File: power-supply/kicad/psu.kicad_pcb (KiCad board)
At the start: 2 copper layers, 22 x 21.6 mm, 13 parts, among them J3 SSQ-103-03-G-D, U1 LM2776, U3 TPS72301DBVR, U5 TPS79333DBVR

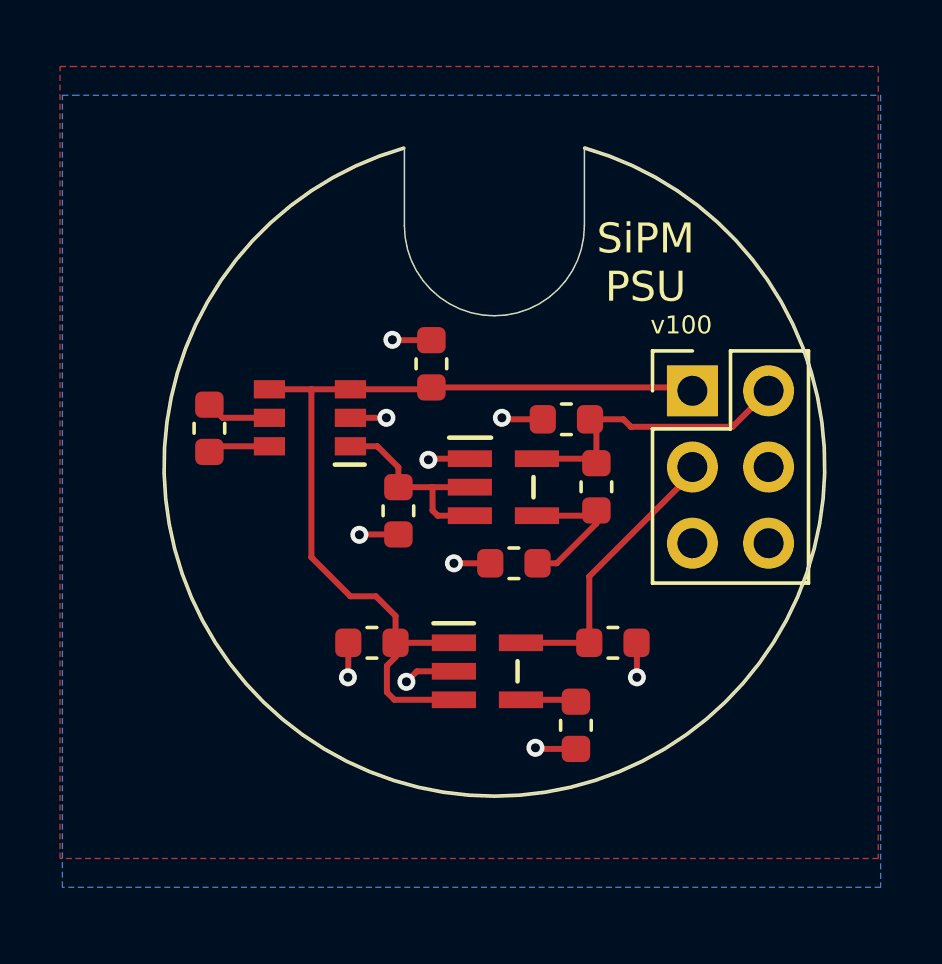
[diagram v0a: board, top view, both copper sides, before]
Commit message: Minor changes to power supply
Changes:

Add LC filter on output of the negative regulator. This is almost certainly not needed, but it further rejects the 2MHz inverting regulator switch frequency.  Replace inductor with a jumper if you don't want to use it.

Clean up traces and layout of existing components.

Widen notch so that SMB cables can fit through more easily.

Adjust negative rail voltage to be -4.5v instead of -3.3v to increase dynamic range.

Move connector so there is a bit more room to fit in lens tube.
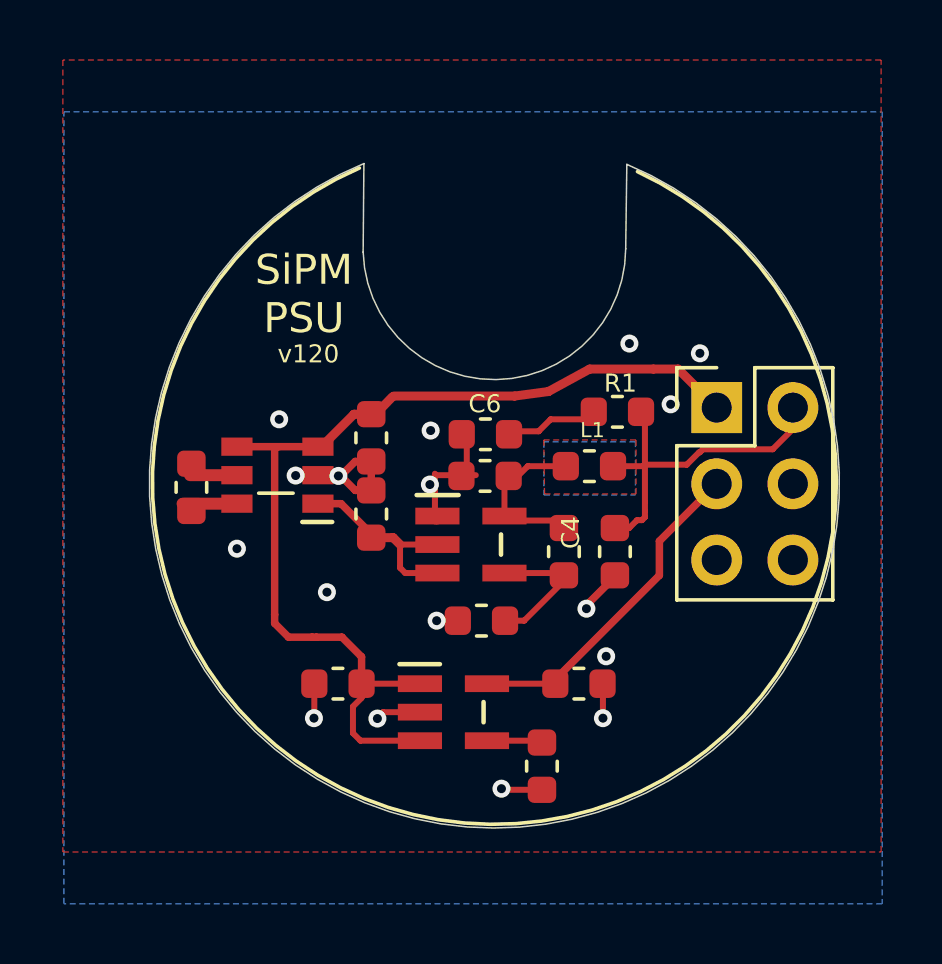
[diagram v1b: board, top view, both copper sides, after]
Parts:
- added C4: 22u, footprints:C_0603_1608Metric, F.Cu at (204.0, 102.9)
- added C6: 22u, footprints:C_0603_1608Metric, F.Cu at (199.7, 99.0)
- added L1: 1uH, footprints:L_0603_1608Metric, F.Cu at (203.2, 100.0)
- added R1: .5, footprints:R_0603_1608Metric, F.Cu at (204.1, 98.2)
- C2: value 10u -> 1u
- C3, C5: value 10u -> 22u
- U3: value TPS72301DBVR -> DBV5
- U5: value TPS79333DBVR -> DBV5
- moved C5 3.30 mm to (199.7, 100.3)
- moved C1 3.18 mm to (195.9, 99.1), turned to 90 degrees
- moved R8 2.42 mm to (202.3, 102.9)
- moved R9 2.20 mm to (199.6, 105.2)
- moved U1 2.20 mm to (192.8, 100.3)
- moved U3 2.20 mm to (199.2, 102.6)
- moved C8 2.06 mm to (189.9, 100.7)
- moved C17 1.77 mm to (201.6, 110.0)
- moved C2 1.77 mm to (194.8, 107.3)
- moved C3 1.77 mm to (202.8, 107.3)
- moved U5 1.77 mm to (198.6, 108.2)
- moved J3 0.98 mm to (207.4, 98.1)
- moved C15 0.91 mm to (195.9, 101.6), turned to -90 degrees
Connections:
- C5 pad 2: VSSA -> Net-(C5-Pad2)
- J3 pad 4: (no net) -> Net-(J3-Pad4)
- J3 pad 5: (no net) -> /BIAS
- R8 pad 2: VSSA -> Net-(C5-Pad2)
- U3 pad 5: VSSA -> Net-(C5-Pad2)
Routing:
- net Net-(C5-Pad2): track 0.00 -> 5.48 mm
- net GND: track 13.3 -> 16.7 mm, vias 10 -> 17
- net Net-(C6-Pad1): track 0.00 -> 3.32 mm
- net +5V: track 30.7 -> 33.6 mm
- net VSSA: track 9.85 -> 12.0 mm
- net VDDA: track 10.7 -> 12.0 mm
- net Net-(C8-Pad2): track 2.38 -> 1.56 mm
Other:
- board size 22 x 21.6 mm -> 23 x 22.1 mm
- net class Default removed
- board text added: "+3.3V"
- board text added: "-4.5V"
- board text added: "Bias"
- board text added: "GND"
- board text added: "USB5V"
- board text added: "v120"
- board text removed: "v100"

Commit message: Lower negative voltage rail slightly
Depending on the USB +5 load, the length of the cable, etc the voltage could dip enough that the regulator would drop out under very heavy load.  Decreasing to 4.3v prevents this but still enables >1.3v output.
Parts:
- C4: value 22u -> 4.7u
- R9: value 36.5k -> 24.9k
- U3: value DBV5 -> TPS72301DBVR
- U5: value DBV5 -> TPS79333DBVR
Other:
- board text added: "-4.3V"
- board text removed: "-4.5V"
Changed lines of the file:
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@@
     (fp_circle (center -0.5461 -0.95) (end -0.4699 -0.95) (layer "F.Fab") (width 0.1524))
     (pad "1" smd rect (at -1.35 -0.950001 180) (size 1.0414 0.6096) (layers "F.Cu" "F.Paste" "F.Mask")
-      (net 4 "-5V"))
+      (net 4 "-5V") (pinfunction "Vout"))
     (pad "2" smd rect (at -1.35 0 180) (size 1.0414 0.6096) (layers "F.Cu" "F.Paste" "F.Mask")
-      (net 1 "GND"))
+      (net 1 "GND") (pinfunction "GND"))
     (pad "3" smd rect (at -1.35 0.950001 180) (size 1.0414 0.6096) (layers "F.Cu" "F.Paste" "F.Mask")
-      (net 2 "+5V"))
+      (net 2 "+5V") (pinfunction "Vin"))
     (pad "4" smd rect (at 1.35 0.950001 180) (size 1.0414 0.6096) (layers "F.Cu" "F.Paste" "F.Mask")
-      (net 2 "+5V"))
+      (net 2 "+5V") (pinfunction "EN"))
     (pad "5" smd rect (at 1.35 0 180) (size 1.0414 0.6096) (layers "F.Cu" "F.Paste" "F.Mask")
-      (net 6 "Net-(C8-Pad2)"))
+      (net 6 "Net-(C8-Pad2)") (pinfunction "C1+"))
     (pad "6" smd rect (at 1.35 -0.950001 180) (size 1.0414 0.6096) (layers "F.Cu" "F.Paste" "F.Mask")
-      (net 7 "Net-(C8-Pad1)"))
+      (net 7 "Net-(C8-Pad1)") (pinfunction "C1-"))
     (model "${KIPRJMOD}/step/DBV6.step"
       (at (xyz 0 0 0))
@@
     (tags "inductor")
     (attr smd)
-    (fp_text reference "L1" (at -0.1 1.2) (layer "F.SilkS")
+    (fp_text reference "L1" (at 0.0176 -0.937499) (layer "F.SilkS")
       (effects (font (size 0.5 0.5) (thickness 0.1)))
     )
@@
     (tags "capacitor")
     (attr smd)
-    (fp_text reference "C4" (at -0.6375 1.475 -90) (layer "F.SilkS")
-      (effects (font (size 0.6 0.6) (thickness 0.1)))
-    )
-    (fp_text value "22u" (at 0 1.43 90) (layer "F.Fab")
+    (fp_text reference "C4" (at 1.962499 0.0426) (layer "F.SilkS")
+      (effects (font (size 0.6 0.6) (thickness 0.1)))
+    )
+    (fp_text value "4.7u" (at 0 1.43 90) (layer "F.Fab")
       (effects (font (size 0.6 0.6) (thickness 0.1)))
     )
@@
       (effects (font (size 1 1) (thickness 0.15)))
     )
-    (fp_text value "DBV5" (at 0 0) (layer "F.SilkS") hide
+    (fp_text value "TPS79333DBVR" (at 0 0) (layer "F.SilkS") hide
       (effects (font (size 1 1) (thickness 0.15)))
     )
@@
     )
     (pad "1" smd rect (at -1.1176 -0.950001) (size 1.4732 0.5588) (layers "F.Cu" "F.Paste" "F.Mask")
-      (net 2 "+5V"))
+      (net 2 "+5V") (pinfunction "IN"))
     (pad "2" smd rect (at -1.1176 0) (size 1.4732 0.5588) (layers "F.Cu" "F.Paste" "F.Mask")
-      (net 1 "GND"))
+      (net 1 "GND") (pinfunction "GND"))
     (pad "3" smd rect (at -1.1176 0.950001) (size 1.4732 0.5588) (layers "F.Cu" "F.Paste" "F.Mask")
-      (net 2 "+5V"))
+      (net 2 "+5V") (pinfunction "EN"))
     (pad "4" smd rect (at 1.1176 0.950001) (size 1.4732 0.5588) (layers "F.Cu" "F.Paste" "F.Mask")
-      (net 8 "Net-(C17-Pad2)"))
+      (net 8 "Net-(C17-Pad2)") (pinfunction "NR"))
     (pad "5" smd rect (at 1.1176 -0.950001) (size 1.4732 0.5588) (layers "F.Cu" "F.Paste" "F.Mask")
-      (net 3 "VDDA"))
+      (net 3 "VDDA") (pinfunction "OUT"))
     (model "${KIPRJMOD}/step/DBV5.step"
       (at (xyz 0 0 0))
@@
       (effects (font (size 1 1) (thickness 0.15)))
     )
-    (fp_text value "DBV5" (at 0 0) (layer "F.SilkS") hide
+    (fp_text value "TPS72301DBVR" (at 0 0) (layer "F.SilkS") hide
       (effects (font (size 1 1) (thickness 0.15)))
     )
@@
     )
     (pad "5" smd rect (at 1.1176 -0.950001) (size 1.4732 0.5588) (layers "F.Cu" "F.Paste" "F.Mask")
-      (net 10 "Net-(C5-Pad2)"))
+      (net 10 "Net-(C5-Pad2)") (pinfunction "OUT"))
     (pad "4" smd rect (at 1.1176 0.950001) (size 1.4732 0.5588) (layers "F.Cu" "F.Paste" "F.Mask")
-      (net 9 "Net-(R8-Pad1)"))
+      (net 9 "Net-(R8-Pad1)") (pinfunction "FB"))
     (pad "3" smd rect (at -1.1176 0.950001) (size 1.4732 0.5588) (layers "F.Cu" "F.Paste" "F.Mask")
-      (net 4 "-5V"))
+      (net 4 "-5V") (pinfunction "EN"))
     (pad "2" smd rect (at -1.1176 0) (size 1.4732 0.5588) (layers "F.Cu" "F.Paste" "F.Mask")
-      (net 4 "-5V"))
+      (net 4 "-5V") (pinfunction "IN"))
     (pad "1" smd rect (at -1.1176 -0.950001) (size 1.4732 0.5588) (layers "F.Cu" "F.Paste" "F.Mask")
-      (net 1 "GND"))
+      (net 1 "GND") (pinfunction "GND"))
     (model "${KIPRJMOD}/step/DBV5.step"
       (at (xyz 0 0 0))
@@
       (effects (font (size 0.6 0.6) (thickness 0.1)))
     )
-    (fp_text value "36.5k" (at 0 1.43) (layer "F.Fab") hide
+    (fp_text value "24.9k" (at 0 1.43) (layer "F.Fab") hide
       (effects (font (size 1 1) (thickness 0.15)))
     )
@@
     (tags "capacitor")
     (attr smd)
-    (fp_text reference "C3" (at -0.6375 1.475 180) (layer "F.SilkS") hide
+    (fp_text reference "C3" (at -0.0074 1.1375 180) (layer "F.SilkS") hide
       (effects (font (size 0.6 0.6) (thickness 0.1)))
     )
@@
     (fp_line (start 0 -1.27) (end 3.81 -1.27) (layer "F.Fab") (width 0.1))
     (pad "6" thru_hole oval (at 2.54 5.08) (size 1.7 1.7) (drill 1) (layers *.Cu *.Mask)
-      (net 1 "GND"))
+      (net 1 "GND") (pinfunction "Pin_6"))
     (pad "5" thru_hole oval (at 0 5.08) (size 1.7 1.7) (drill 1) (layers *.Cu *.Mask)
-      (net 11 "/BIAS"))
+      (net 11 "/BIAS") (pinfunction "Pin_5"))
     (pad "4" thru_hole oval (at 2.54 2.54) (size 1.7 1.7) (drill 1) (layers *.Cu *.Mask)
-      (net 12 "Net-(J3-Pad4)"))
+      (net 12 "Net-(J3-Pad4)") (pinfunction "Pin_4"))
     (pad "3" thru_hole oval (at 0 2.54) (size 1.7 1.7) (drill 1) (layers *.Cu *.Mask)
-      (net 3 "VDDA"))
+      (net 3 "VDDA") (pinfunction "Pin_3"))
     (pad "2" thru_hole oval (at 2.54 0) (size 1.7 1.7) (drill 1) (layers *.Cu *.Mask)
-      (net 5 "VSSA"))
+      (net 5 "VSSA") (pinfunction "Pin_2"))
     (pad "1" thru_hole rect (at 0 0) (size 1.7 1.7) (drill 1) (layers *.Cu *.Mask)
-      (net 2 "+5V"))
+      (net 2 "+5V") (pinfunction "Pin_1"))
     (model "${KIPRJMOD}/step/SSQ-103-03-G-D.step"
       (offset (xyz 1.25 -2.5 0))
@@
     (effects (font (size 1 1) (thickness 0.15)) (justify mirror))
   )
-  (gr_text "-4.5V" (at 209.3 96.1) (layer "B.SilkS")
+  (gr_text "-4.3V" (at 209.3 96.1) (layer "B.SilkS")
     (effects (font (size 0.6 0.6) (thickness 0.15)) (justify mirror))
   )

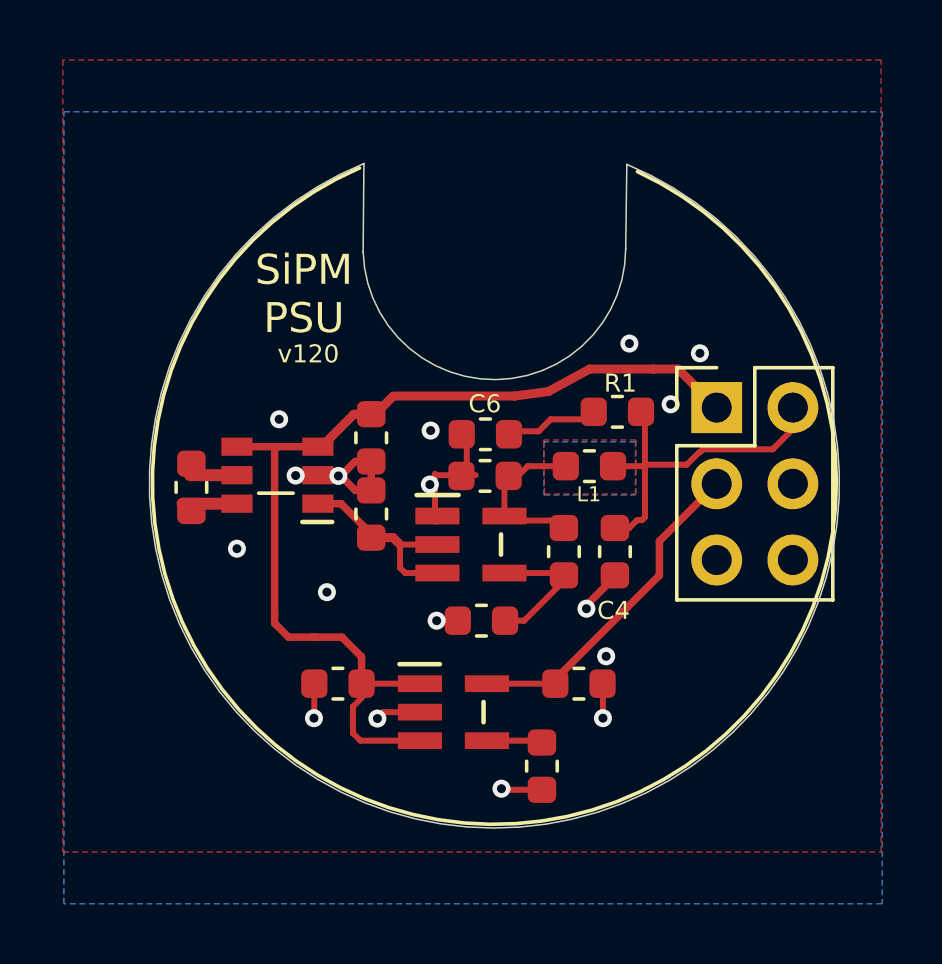
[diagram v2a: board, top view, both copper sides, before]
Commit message: Slightly improve routing around the nedative power supply
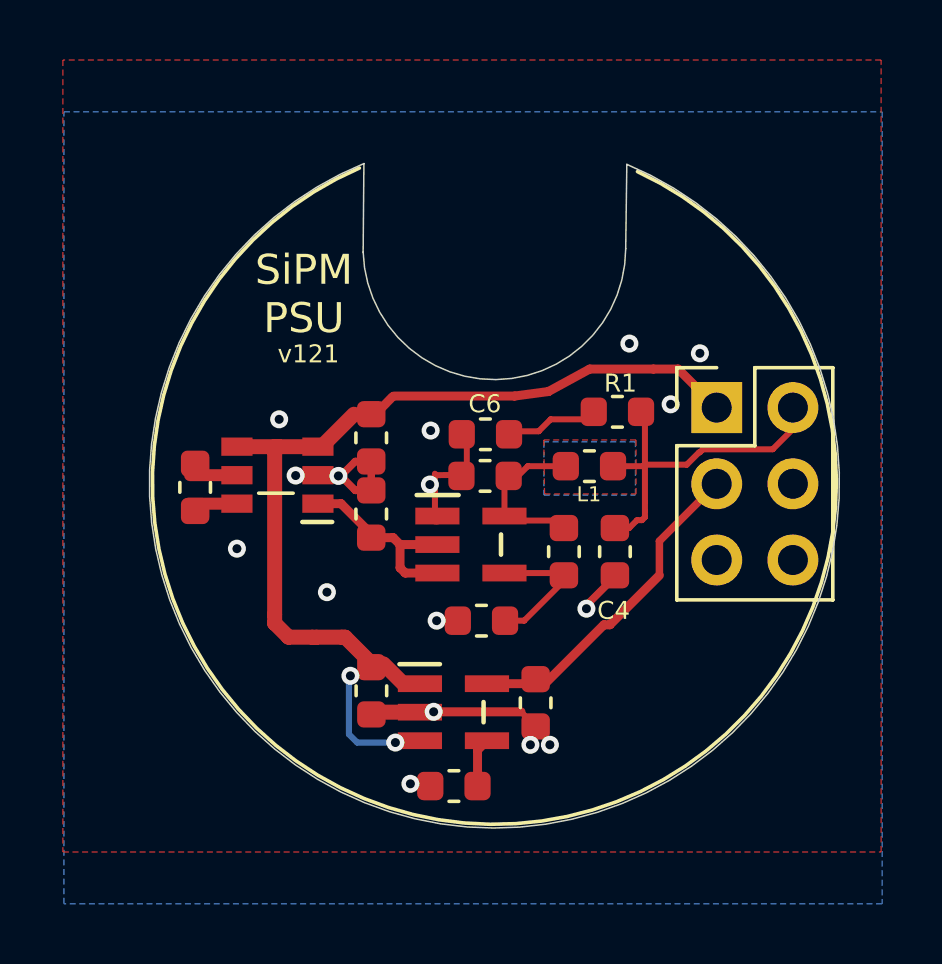
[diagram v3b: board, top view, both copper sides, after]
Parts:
- moved C17 3.01 mm to (198.7, 110.7), turned to 0 degrees
- moved C3 1.58 mm to (201.4, 107.9), turned to 90 degrees
- moved C2 1.14 mm to (195.9, 107.5), turned to 90 degrees
- moved C8 0.12 mm to (190.0, 100.7)
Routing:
- net GND: track 16.7 -> 15.8 mm, vias 17 -> 16
- net +5V: track 33.6 -> 32.9 mm, vias 0 -> 2
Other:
- board text added: "v121"
- board text removed: "v120"

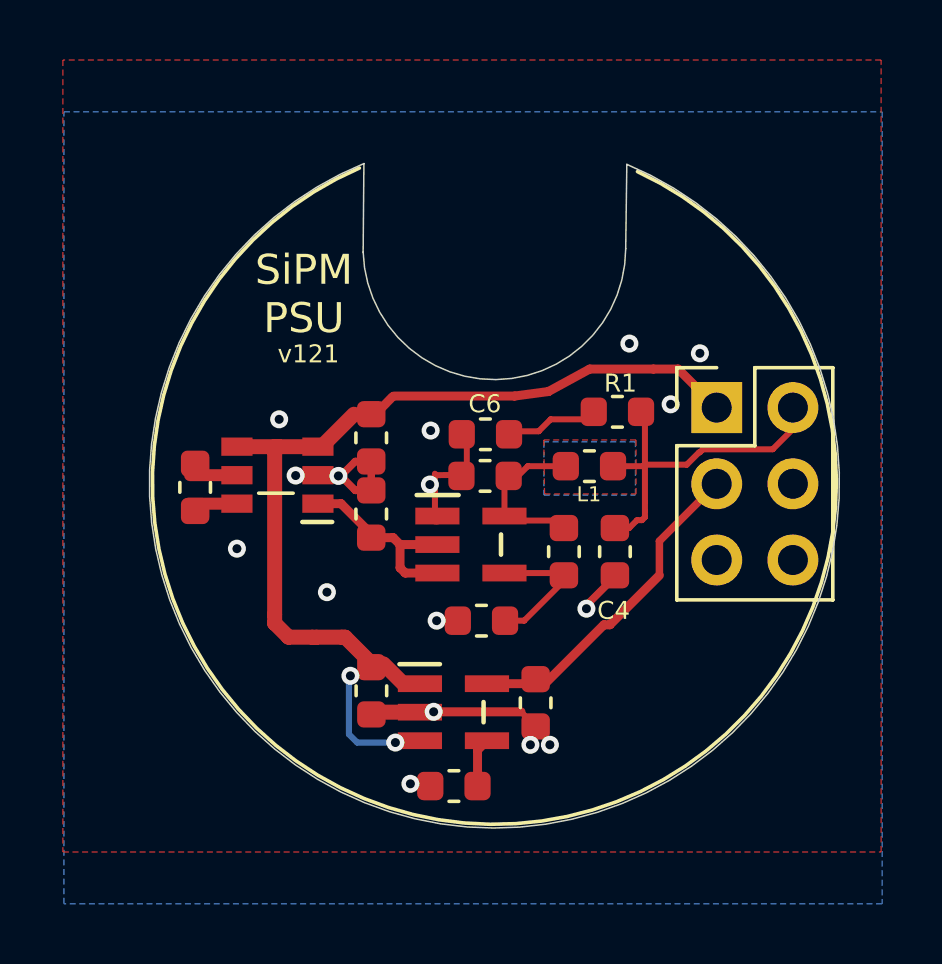
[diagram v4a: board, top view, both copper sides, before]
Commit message: Remove unneeded LC filter from power supply negative rail
In testing it made no difference and complicated the layout.
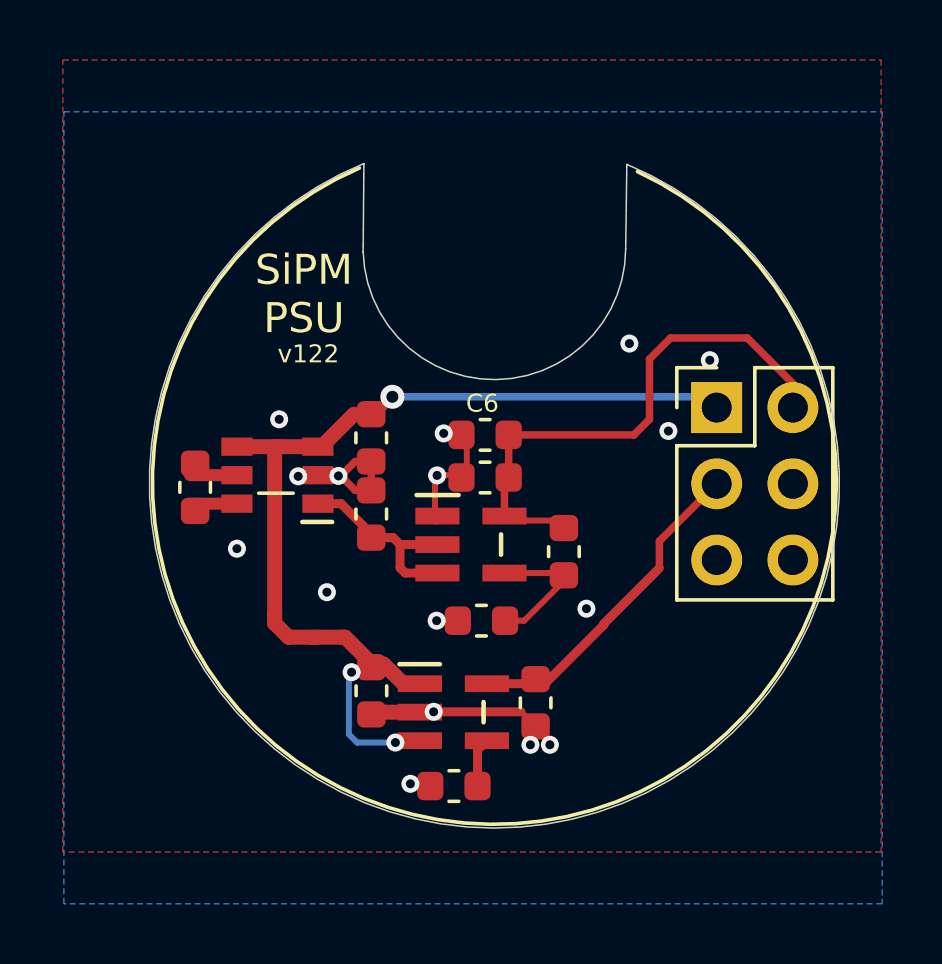
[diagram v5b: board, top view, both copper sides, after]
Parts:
- removed C4: 4.7u, footprints:C_0603_1608Metric
- removed L1: 1uH, footprints:L_0603_1608Metric
- removed R1: .5, footprints:R_0603_1608Metric
- moved C5 0.05 mm to (199.7, 100.4)
- turned C6 to 0 degrees
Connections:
- C5 pad 2: Net-(C5-Pad2) -> VSSA
- C6 pad 1: Net-(C6-Pad1) -> GND
- C6 pad 2: GND -> VSSA
- J3 pad 4: Net-(J3-Pad4) -> (no net)
- J3 pad 5: /BIAS -> (no net)
- R8 pad 2: Net-(C5-Pad2) -> VSSA
- U3 pad 5: Net-(C5-Pad2) -> VSSA
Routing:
- net VSSA: track 12.0 -> 18.3 mm
- net Net-(C5-Pad2): track 5.48 -> 0.00 mm
- net Net-(C6-Pad1): track 3.32 -> 0.00 mm
- net GND: track 15.8 -> 14.4 mm
- net +5V: track 32.9 -> 32.4 mm, vias 2 -> 3
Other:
- board text added: "v122"
- board text removed: "v121"
